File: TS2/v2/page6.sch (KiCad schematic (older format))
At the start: 23 parts, among them SW2 SINGLE STEP/RUN, SW3 STEP, U10 74LS32, U19 74LS20, U20 74LS74, U21 74LS161, U22 74LS161, U23 74LS74, U4 74LS06, U5 74LS04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

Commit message: Add some internal signal names.
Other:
- note added: "(DTACK* generated in single step mode)"
- note added: "INHIBIT_DTACK"
- note added: "MSEL"
- note added: "SS_DTACK*"
- note removed: "DTACK* generated in single step mode"
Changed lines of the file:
@@
 Sheet 7 9
 Title "TS2 68000 Single Board Computer"
-Date "2017-01-05"
+Date "2017-01-14"
 Rev "2.0"
 Comp "Jeff Tranter"
@@
 Text Notes 3550 7400 0    60   ~ 0
 Watchdog timer
-Text Notes 5350 5000 0    60   ~ 0
-DTACK* generated in single step mode
+Text Notes 5000 5250 0    60   ~ 0
+(DTACK* generated in single step mode)
 Text Notes 650  5900 0    60   ~ 0
 A single bus cycle\nis executed each\ntime the STEP switch\nis pushed
@@
 Wire Wire Line
 	3400 2000 3400 2300
+Text Notes 2550 1950 0    60   ~ 0
+MSEL
+Text Notes 4850 3500 0    60   ~ 0
+INHIBIT_DTACK
+Text Notes 5050 5050 0    60   ~ 0
+SS_DTACK*
 $EndSCHEMATC

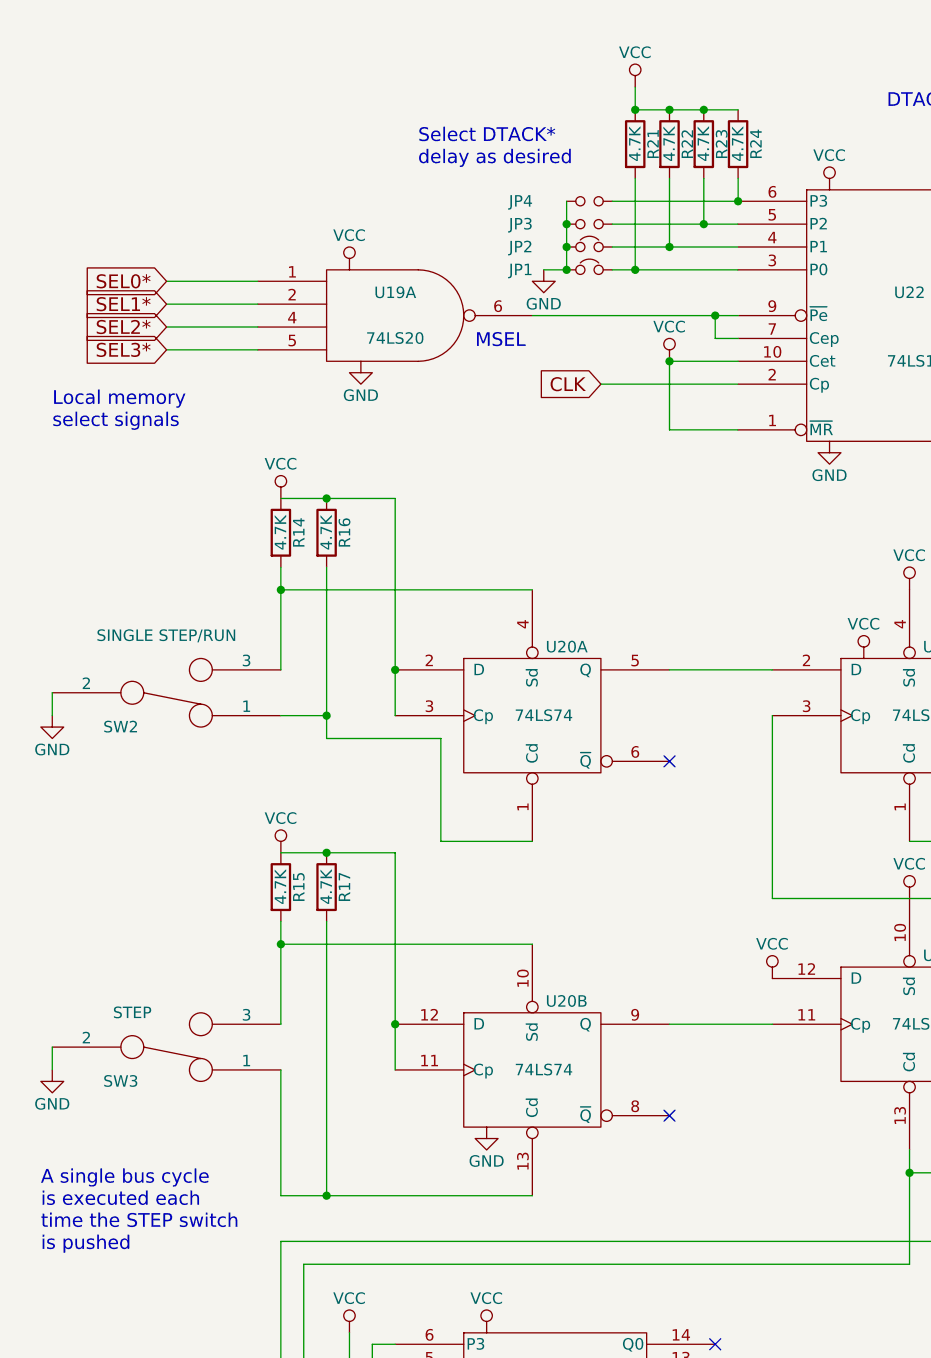
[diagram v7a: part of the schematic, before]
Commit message: Add all bypass caps, show pullups as SIP resistors, start PCB layout.
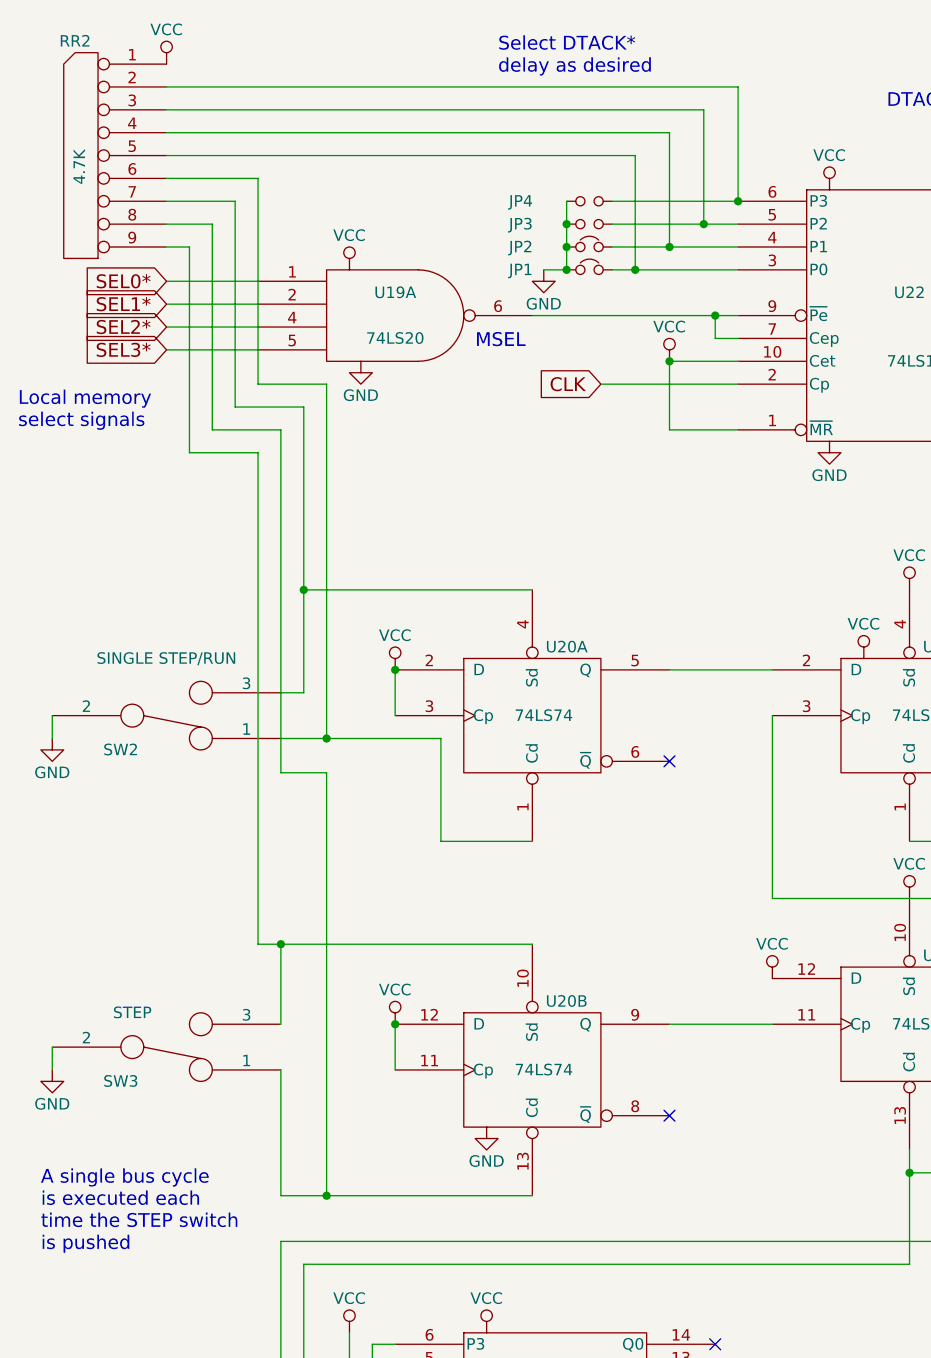
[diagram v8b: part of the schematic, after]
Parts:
- removed R14, R15, R16, R17, R21, R22, R23, R24: 4.7K, symbol R
- added RR2: 4.7K, Resistors_ThroughHole:Resistor_Array_SIP8, symbol RR8
- JP1, JP2, JP3, JP4: footprint (none) -> Buttons_Switches_ThroughHole:SW_DIP_x1_Slide
- SW2, SW3: footprint (none) -> Connect:PINHEAD1-3
- U10, U19, U20, U23, U4, U5, U7: footprint (none) -> Housings_DIP:DIP-14_W7.62mm
- U21, U22: footprint (none) -> Housings_DIP:DIP-16_W7.62mm
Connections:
- net VCC: now also RR2.1 (COM)
- net at JP1.2, U22.3 (P0): now also RR2.5
- net at JP2.2, U22.4 (P1): now also RR2.4
- net at JP3.2, U22.5 (P2): now also RR2.3
- net at JP4.2, U22.6 (P3): now also RR2.2
- net at SW2.1, U20.1 (Cd): now also RR2.6
- net at SW2.3, U20.4 (Sd): now also RR2.7
- net at SW3.3, U20.10 (Sd): now also RR2.9
- net at SW3.1, U20.13 (Cd): now also RR2.8
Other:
- moved on the sheet: SW2
